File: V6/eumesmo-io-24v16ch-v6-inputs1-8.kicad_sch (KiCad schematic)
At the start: 10 parts, among them U12 OR-3H7-4

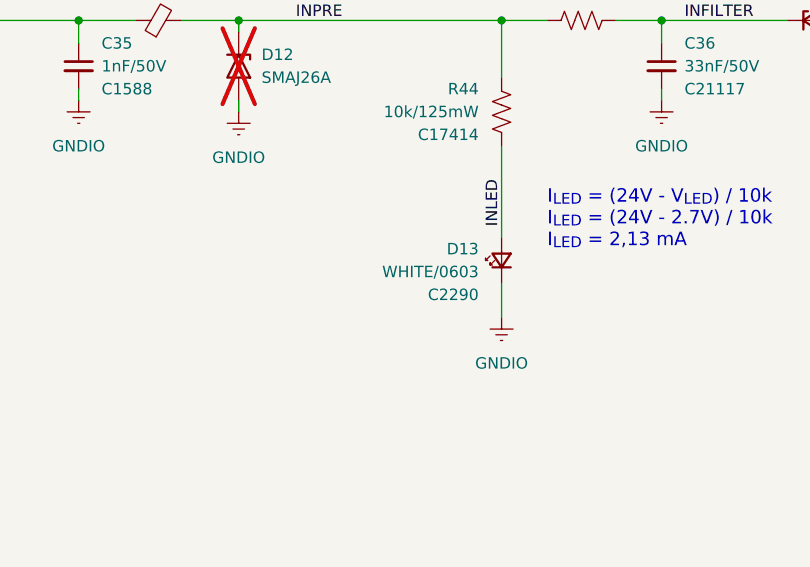
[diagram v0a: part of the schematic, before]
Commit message: Replaced white leds for emerald.
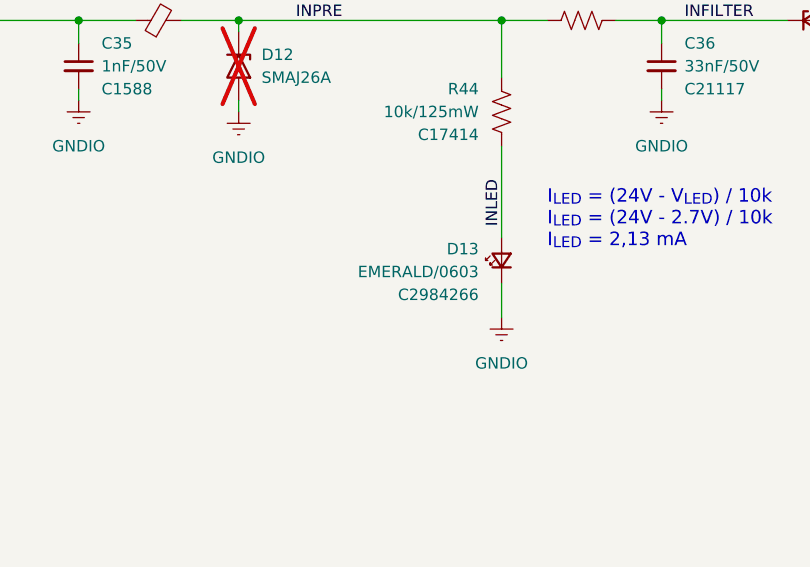
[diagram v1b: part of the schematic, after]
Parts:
- D13: value WHITE/0603 -> EMERALD/0603; LCSC Part # C2290 -> C2984266; Mfr Hubei KENTO Elec -> Everlight Elec; Mfr PN KT-0603W -> 19-213/GHC-XS1T1N/5T; Technology (none) -> LED; Vendor PN C2290 -> C2984266
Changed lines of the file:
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@@
 			)
 		)
-		(property "Value" "WHITE/0603"
+		(property "Value" "EMERALD/0603"
 			(at 123.19 120.65 90)
 			(show_name no)
@@
 			)
 		)
-		(property "Mfr" "Hubei KENTO Elec"
+		(property "Mfr" "Everlight Elec"
 			(at 125.73 119.38 0)
 			(hide yes)
@@
 			)
 		)
-		(property "Mfr PN" "KT-0603W"
+		(property "Mfr PN" "19-213/GHC-XS1T1N/5T"
 			(at 125.73 119.38 0)
 			(hide yes)
@@
 			)
 		)
-		(property "Technology" ""
+		(property "Technology" "LED"
 			(at 125.73 119.38 0)
 			(hide yes)
@@
 			)
 		)
-		(property "Vendor PN" "C2290"
+		(property "Vendor PN" "C2984266"
 			(at 125.73 119.38 0)
 			(hide yes)
@@
 			)
 		)
-		(property "LCSC Part #" "C2290"
+		(property "LCSC Part #" "C2984266"
 			(at 123.19 123.19 90)
 			(show_name no)

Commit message: Remove jumpers from BOM.
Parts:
- D13: FT Rotation Offset 0 -> 180
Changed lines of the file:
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@@
 			)
 		)
-		(property "FT Rotation Offset" "0"
+		(property "FT Rotation Offset" "180"
 			(at 125.73 119.38 90)
 			(hide yes)

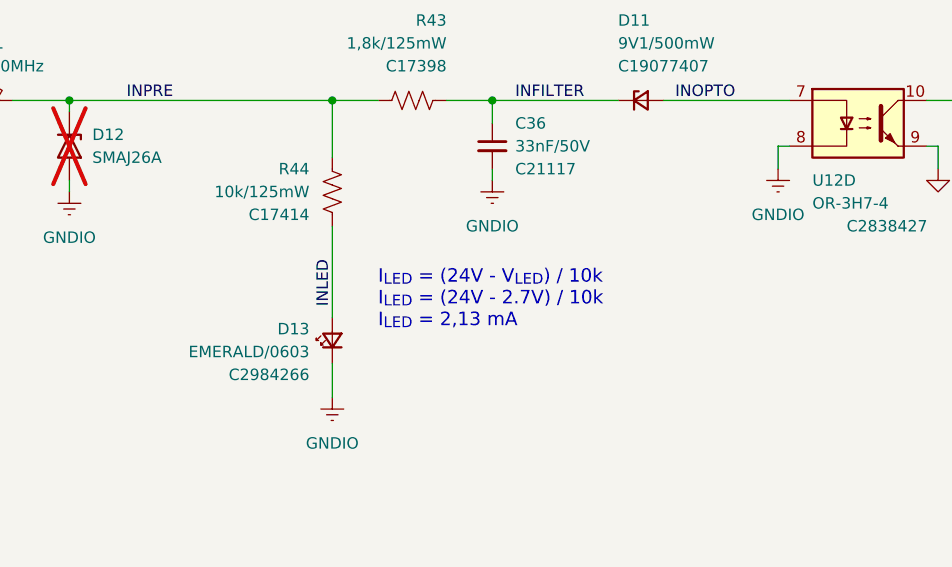
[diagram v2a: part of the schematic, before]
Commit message: LEDs changed to orange
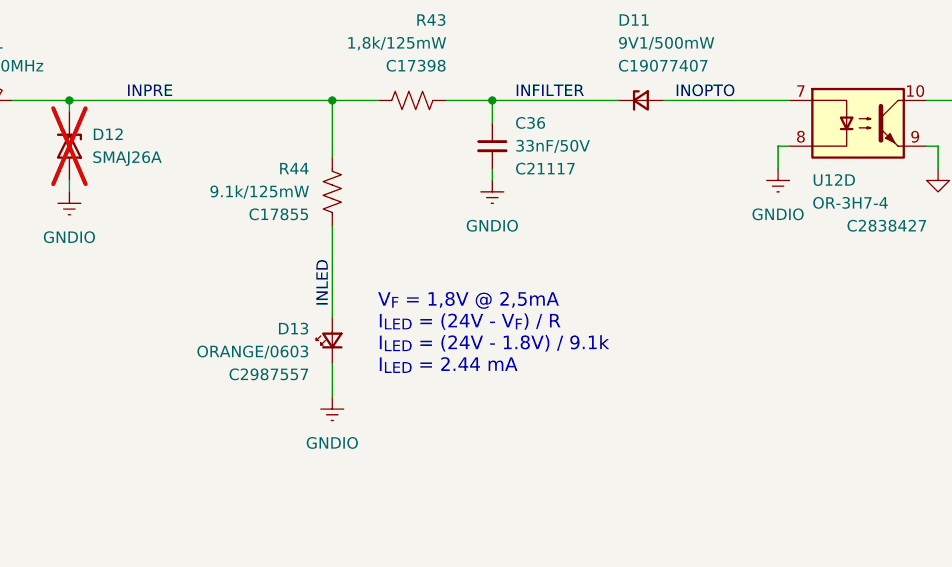
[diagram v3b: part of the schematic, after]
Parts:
- D13: value EMERALD/0603 -> ORANGE/0603; FT Rotation Offset 180 -> 0; LCSC Part # C2984266 -> C2987557; Mfr PN 19-213/GHC-XS1T1N/5T -> 19-217/S2C-AL1M2VY/6T; Vendor PN C2984266 -> C2987557
- R44: value 10k/125mW -> 9.1k/125mW; LCSC Part # C17414 -> C17855; Mfr PN 0805W8F1002T5E -> 0805W8F9101T5E; Vendor PN C17414 -> C17855
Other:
- note added: "V_{F} = 1,8V @ 2,5mA I_{LED} = (24V - V_{F}) / R I_{LED} = (24V - 1.8V) / 9.1k I_{LED} = 2.44 mA"
- note removed: "I_{LED} = (24V - V_{LED}) / 10k I_{LED} = (24V - 2.7V) / 10k I_{LED} = 2,13 mA"
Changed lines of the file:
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@@
 		(rev "V6.3")
 	)
-	(text "I_{LED} = (24V - V_{LED}) / 10k\nI_{LED} = (24V - 2.7V) / 10k\nI_{LED} = 2,13 mA"
+	(text "V_{F} = 1,8V @ 2,5mA\nI_{LED} = (24V - V_{F}) / R\nI_{LED} = (24V - 1.8V) / 9.1k\nI_{LED} = 2.44 mA"
 		(exclude_from_sim no)
-		(at 130.81 118.11 0)
+		(at 130.81 123.19 0)
 		(effects
 			(font
@@
 			)
 		)
-		(property "Value" "EMERALD/0603"
+		(property "Value" "ORANGE/0603"
 			(at 123.19 120.65 90)
 			(show_name no)
@@
 			)
 		)
-		(property "Mfr PN" "19-213/GHC-XS1T1N/5T"
+		(property "Mfr PN" "19-217/S2C-AL1M2VY/6T"
 			(at 125.73 119.38 0)
 			(hide yes)
@@
 			)
 		)
-		(property "Vendor PN" "C2984266"
+		(property "Vendor PN" "C2987557"
 			(at 125.73 119.38 0)
 			(hide yes)
@@
 			)
 		)
-		(property "LCSC Part #" "C2984266"
+		(property "LCSC Part #" "C2987557"
 			(at 123.19 123.19 90)
 			(show_name no)
@@
 			)
 		)
-		(property "FT Rotation Offset" "180"
+		(property "FT Rotation Offset" "0"
 			(at 125.73 119.38 90)
 			(hide yes)
@@
 			)
 		)
-		(property "Value" "10k/125mW"
+		(property "Value" "9.1k/125mW"
 			(at 123.19 102.87 0)
 			(show_name no)
@@
 			)
 		)
-		(property "Mfr PN" "0805W8F1002T5E"
+		(property "Mfr PN" "0805W8F9101T5E"
 			(at 125.73 102.87 0)
 			(hide yes)
@@
 			)
 		)
-		(property "Vendor PN" "C17414"
+		(property "Vendor PN" "C17855"
 			(at 125.73 102.87 0)
 			(hide yes)
@@
 			)
 		)
-		(property "LCSC Part #" "C17414"
+		(property "LCSC Part #" "C17855"
 			(at 123.19 105.41 0)
 			(show_name no)

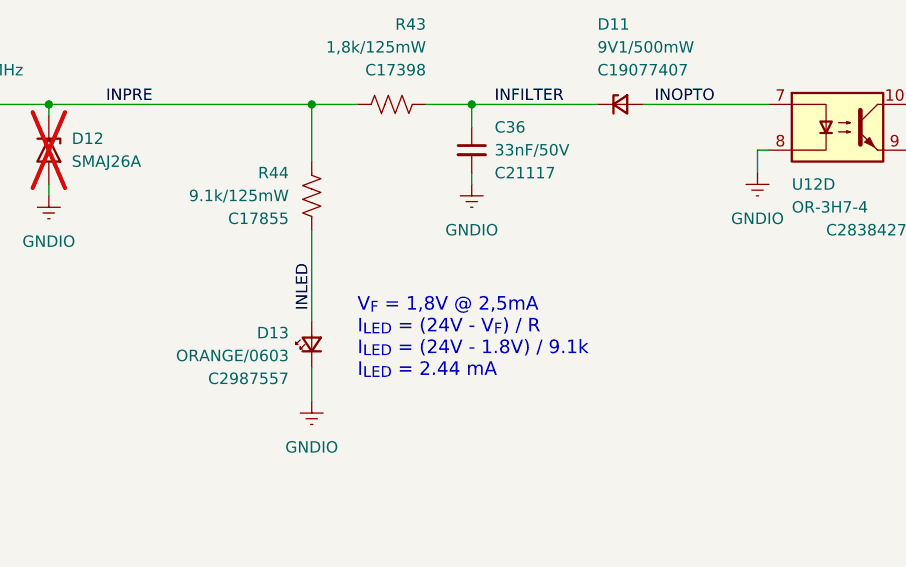
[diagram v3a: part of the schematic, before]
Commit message: LEDs replaced for orange
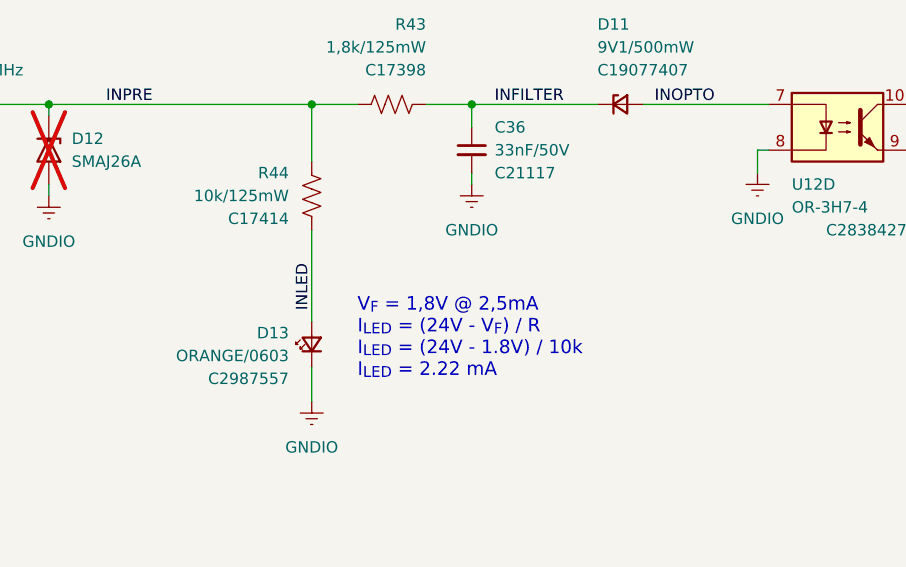
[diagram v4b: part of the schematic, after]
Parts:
- R44: value 9.1k/125mW -> 10k/125mW; LCSC Part # C17855 -> C17414; Mfr PN 0805W8F9101T5E -> 0805W8F1002T5E; Vendor PN C17855 -> C17414
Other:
- note added: "V_{F} = 1,8V @ 2,5mA I_{LED} = (24V - V_{F}) / R I_{LED} = (24V - 1.8V) / 10k I_{LED} = 2.22 mA"
- note removed: "V_{F} = 1,8V @ 2,5mA I_{LED} = (24V - V_{F}) / R I_{LED} = (24V - 1.8V) / 9.1k I_{LED} = 2.44 mA"
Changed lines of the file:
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@@
 		(rev "V6.3")
 	)
-	(text "V_{F} = 1,8V @ 2,5mA\nI_{LED} = (24V - V_{F}) / R\nI_{LED} = (24V - 1.8V) / 9.1k\nI_{LED} = 2.44 mA"
+	(text "V_{F} = 1,8V @ 2,5mA\nI_{LED} = (24V - V_{F}) / R\nI_{LED} = (24V - 1.8V) / 10k\nI_{LED} = 2.22 mA"
 		(exclude_from_sim no)
 		(at 130.81 123.19 0)
@@
 			)
 		)
-		(property "Value" "9.1k/125mW"
+		(property "Value" "10k/125mW"
 			(at 123.19 102.87 0)
 			(show_name no)
@@
 			)
 		)
-		(property "Mfr PN" "0805W8F9101T5E"
+		(property "Mfr PN" "0805W8F1002T5E"
 			(at 125.73 102.87 0)
 			(hide yes)
@@
 			)
 		)
-		(property "Vendor PN" "C17855"
+		(property "Vendor PN" "C17414"
 			(at 125.73 102.87 0)
 			(hide yes)
@@
 			)
 		)
-		(property "LCSC Part #" "C17855"
+		(property "LCSC Part #" "C17414"
 			(at 123.19 105.41 0)
 			(show_name no)
